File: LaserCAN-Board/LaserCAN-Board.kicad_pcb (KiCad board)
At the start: 4 copper layers, 25 x 25 mm, 58 parts, among them J2 TC2050-IDC-NL, Q1 Si2309CDS-T1-GE3, U1 TPS7A2033PDBVR, U2 VL53L1CXV0FY1, U3 M24C64-RMN6TP, U4 STM32F103C8Tx, U6 SN65HVD230, U9 TPS54202DDC, Y1 8MHz 20pF

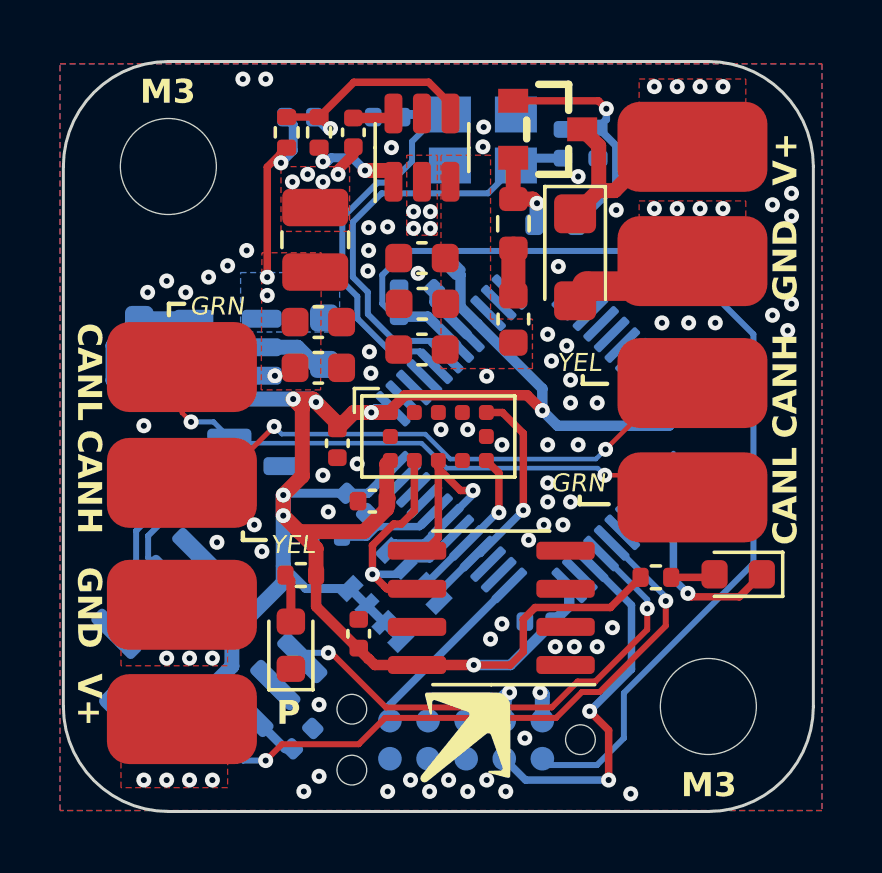
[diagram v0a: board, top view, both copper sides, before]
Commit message: Rev 4 updates - NPTH, improved routing, BOM optimisation
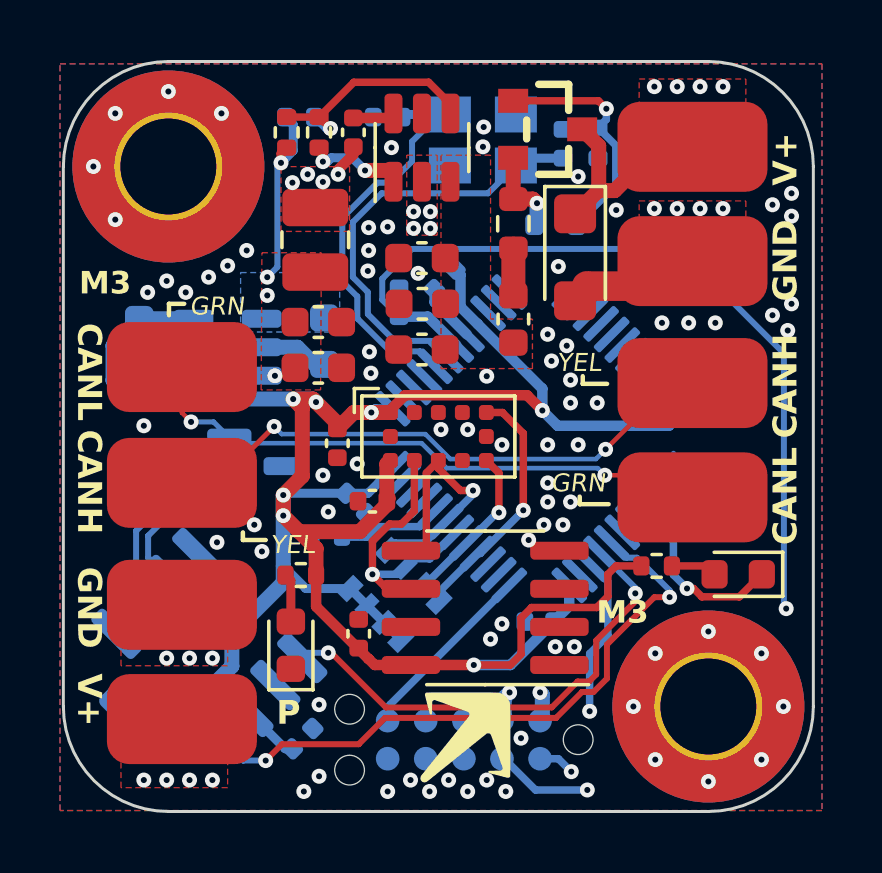
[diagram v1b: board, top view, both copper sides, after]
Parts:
- C20, C21: value 33pF -> 20pF
- H1, H2: footprint MountingHole:MountingHole_3.2mm_M3 -> MountingHole:MountingHole_3.2mm_M3_Pad_TopBottom
- Y1: value 8MHz 20pF -> 8MHz 12pF
- moved R6 0.38 mm to (139.8, 116.8)
- moved U3 0.20 mm to (134.1, 118.2)
- moved J2 0.08 mm to (135.9, 123.2)
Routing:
- net /NRST: track 36.1 -> 40.2 mm, vias 0 -> 2
- net /SWDIO: track 12.4 -> 11.8 mm
- net +3V3: track 88.8 -> 89.4 mm
- net /3V87: track 8.19 -> 7.60 mm
- net unconnected-(H2-Pad1): vias 0 -> 8
- net unconnected-(H1-Pad1): vias 0 -> 5
- net GND: vias 72 -> 67

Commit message: Start working on Rev5
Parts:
- R9: value 4.7 100mW -> 4.7
- moved RN1 0.52 mm to (130.6, 118.0)
- moved R10 0.18 mm to (128.7, 115.7)
- moved D4 0.08 mm to (126.5, 113.4)
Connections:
- net /SWDIO renamed /SWDIO/JTMS
- J2 pad 1: /NRST -> +12V
- J2 pad 10: +12V -> /NRST
- J2 pad 4: GND -> /SWCLK/JTCK
- J2 pad 6: /SWCLK -> /JTDO
- J2 pad 8: unconnected-(J2-Pad8) -> /JTDI
- J2 pad 9: +12V -> unconnected-(J2-Pad9)
- U4 pad 3: unconnected-(U4-PC14-Pad3) -> GND
- U4 pad 37: /SWCLK -> /SWCLK/JTCK
- U4 pad 38: unconnected-(U4-PA15-Pad38) -> /JTDI
- U4 pad 39: unconnected-(U4-PB3-Pad39) -> /JTDO
- U4 pad 40: /TOF_SHUT -> unconnected-(U4-PB4-Pad40)
- U4 pad 45: unconnected-(U4-PB8-Pad45) -> /TOF_SHUT
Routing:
- net /JTDI: track 0.00 -> 12.8 mm, vias 0 -> 1
- net /SWCLK/JTCK: track 0.00 -> 11.7 mm, vias 0 -> 3
- net /JTDO: track 0.00 -> 10.7 mm, vias 0 -> 1
- net /SWCLK: track 6.16 -> 0.00 mm
- net /TOF_SHUT: track 8.33 -> 12.7 mm, vias 1 -> 2
- net /NRST: track 40.2 -> 37.6 mm
- net +12V: track 65.9 -> 64.9 mm, vias 10 -> 9
- net /SWDIO/JTMS: track 11.8 -> 10.8 mm, vias 2 -> 1
- net /I2C_SCL: track 9.95 -> 10.8 mm
- net /I2C_SDA: track 8.64 -> 9.54 mm
- net /CAN_TX: track 16.1 -> 15.4 mm
- net +3V3: track 89.4 -> 88.8 mm
- net /TOF_INT: track 5.46 -> 6.03 mm
- net GND: vias 67 -> 62
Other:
- board text added: "LaserCAN Rev. 5"
- board text removed: "LaserCAN Rev. 4"

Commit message: Rev 5 Updates
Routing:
- net /JTDI: track 12.8 -> 5.53 mm, vias 1 -> 0
- net /SWCLK/JTCK: track 11.7 -> 7.47 mm, vias 3 -> 2
- net /JTDO: track 10.7 -> 6.60 mm, vias 1 -> 0
- net /SWDIO/JTMS: track 10.8 -> 9.81 mm, vias 1 -> 0
- net GND: vias 62 -> 64
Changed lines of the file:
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@@
   (via (at 123.444 107.315) (size 0.5) (drill 0.2) (layers "F.Cu" "B.Cu") (free) (net 1))
   (via (at 136.144 112.776) (size 0.5) (drill 0.2) (layers "F.Cu" "B.Cu") (free) (net 1))
+  (via (at 128.397 124.079) (size 0.5) (drill 0.2) (layers "F.Cu" "B.Cu") (free) (net 1))
   (via (at 143.637 108.458) (size 0.5) (drill 0.2) (layers "F.Cu" "B.Cu") (free) (net 1))
   (via (at 136.271 109.982) (size 0.5) (drill 0.2) (layers "F.Cu" "B.Cu") (free) (net 1))
@@
   (via (at 128.651 113.792) (size 0.5) (drill 0.2) (layers "F.Cu" "B.Cu") (free) (net 1))
   (via (at 133.096 123.952) (size 0.5) (drill 0.2) (layers "F.Cu" "B.Cu") (free) (net 1))
+  (via (at 138.176 124.079) (size 0.5) (drill 0.2) (layers "F.Cu" "B.Cu") (free) (net 1))
   (via (at 134.112 110.49) (size 0.5) (drill 0.2) (layers "F.Cu" "B.Cu") (free) (net 1))
   (via (at 136.398 119.507) (size 0.5) (drill 0.2) (layers "F.Cu" "B.Cu") (free) (net 1))
@@
   (via (at 140.462 100.838) (size 0.5) (drill 0.2) (layers "F.Cu" "B.Cu") (free) (net 3))
   (via (at 136.017 123.952) (size 0.5) (drill 0.2) (layers "F.Cu" "B.Cu") (net 3))
-  (segment (start 127.9457 122.6253) (end 127.504813 123.066187) (width 0.5) (layer "In2.Cu") (net 3))
+  (segment (start 128.293903 122.6253) (end 126.967203 123.952) (width 0.5) (layer "In2.Cu") (net 3))
+  (segment (start 135.27 123.205) (end 131.4718 123.205) (width 0.5) (layer "In2.Cu") (net 3))
   (segment (start 120.65 122.174) (end 120.65 107.823) (width 0.5) (layer "In2.Cu") (net 3))
-  (segment (start 127.124052 123.795151) (end 126.267849 123.795151) (width 0.5) (layer "In2.Cu") (net 3))
-  (segment (start 126.111 123.952) (end 124.968 123.952) (width 0.5) (layer "In2.Cu") (net 3))
-  (segment (start 127.504813 123.066187) (end 127.504813 123.41439) (width 0.5) (layer "In2.Cu") (net 3))
   (segment (start 120.65 107.823) (end 122.57 105.903) (width 0.5) (layer "In2.Cu") (net 3))
+  (segment (start 131.4718 123.205) (end 130.8921 122.6253) (width 0.5) (layer "In2.Cu") (net 3))
   (segment (start 125.8928 104.404162) (end 125.8928 102.580199) (width 0.5) (layer "In2.Cu") (net 3))
-  (segment (start 130.8921 122.6253) (end 127.9457 122.6253) (width 0.5) (layer "In2.Cu") (net 3))
-  (segment (start 135.27 123.205) (end 131.4718 123.205) (width 0.5) (layer "In2.Cu") (net 3))
   (segment (start 124.393962 105.903) (end 125.8928 104.404162) (width 0.5) (layer "In2.Cu") (net 3))
   (segment (start 124.968 123.952) (end 122.428 123.952) (width 0.5) (layer "In2.Cu") (net 3))
   (segment (start 122.428 123.952) (end 120.65 122.174) (width 0.5) (layer "In2.Cu") (net 3))
-  (segment (start 131.4718 123.205) (end 130.8921 122.6253) (width 0.5) (layer "In2.Cu") (net 3))
+  (segment (start 126.967203 123.952) (end 124.968 123.952) (width 0.5) (layer "In2.Cu") (net 3))
   (segment (start 127.635 100.838) (end 141.986 100.838) (width 0.5) (layer "In2.Cu") (net 3))
   (segment (start 136.017 123.952) (end 135.27 123.205) (width 0.5) (layer "In2.Cu") (net 3))
-  (segment (start 126.267849 123.795151) (end 126.111 123.952) (width 0.5) (layer "In2.Cu") (net 3))
-  (segment (start 127.504813 123.41439) (end 127.124052 123.795151) (width 0.5) (layer "In2.Cu") (net 3))
+  (segment (start 130.8921 122.6253) (end 128.293903 122.6253) (width 0.5) (layer "In2.Cu") (net 3))
   (segment (start 122.57 105.903) (end 124.393962 105.903) (width 0.5) (layer "In2.Cu") (net 3))
   (segment (start 125.8928 102.580199) (end 127.635 100.838) (width 0.5) (layer "In2.Cu") (net 3))
@@
   (segment (start 130.46037 115.50374) (end 130.109686 115.854424) (width 0.25) (layer "B.Cu") (net 13))
   (segment (start 131.873 115.50374) (end 130.46037 115.50374) (width 0.25) (layer "B.Cu") (net 13))
-  (via (at 135.128 123.9843) (size 0.5) (drill 0.2) (layers "F.Cu" "B.Cu") (net 15))
   (segment (start 138.43 118.783449) (end 138.43 117.613074) (width 0.1524) (layer "B.Cu") (net 15))
   (segment (start 137.198449 120.015) (end 138.43 118.783449) (width 0.1524) (layer "B.Cu") (net 15))
   (segment (start 134.62 123.2408) (end 134.0003 122.6211) (width 0.1524) (layer "B.Cu") (net 15))
   (segment (start 135.699411 120.015) (end 137.198449 120.015) (width 0.1524) (layer "B.Cu") (net 15))
-  (segment (start 134.62 123.2408) (end 134.62 123.4763) (width 0.1524) (layer "B.Cu") (net 15))
   (segment (start 138.43 117.613074) (end 137.570495 116.753569) (width 0.1524) (layer "B.Cu") (net 15))
-  (segment (start 134.62 123.4763) (end 135.128 123.9843) (width 0.1524) (layer "B.Cu") (net 15))
   (segment (start 134.0003 122.6211) (end 134.0003 121.714111) (width 0.1524) (layer "B.Cu") (net 15))
   (segment (start 134.0003 121.714111) (end 135.699411 120.015) (width 0.1524) (layer "B.Cu") (net 15))
@@
   (segment (start 132.851 119.488129) (end 133.721129 118.618) (width 0.2) (layer "F.Cu") (net 36))
   (via (at 132.851 119.488129) (size 0.5) (drill 0.2) (layers "F.Cu" "B.Cu") (net 36))
-  (via (at 128.471459 124.200025) (size 0.5) (drill 0.2) (layers "F.Cu" "B.Cu") (net 36))
   (via (at 133.731 118.618) (size 0.5) (drill 0.2) (layers "F.Cu" "B.Cu") (net 36))
   (segment (start 131.445 120.894129) (end 131.445 122.6058) (width 0.1524) (layer "B.Cu") (net 36))
-  (segment (start 128.713934 124.4425) (end 130.8783 124.4425) (width 0.1524) (layer "B.Cu") (net 36))
   (segment (start 131.445 122.6058) (end 132.08 123.2408) (width 0.1524) (layer "B.Cu") (net 36))
-  (segment (start 130.8783 124.4425) (end 132.08 123.2408) (width 0.1524) (layer "B.Cu") (net 36))
-  (segment (start 128.471459 124.200025) (end 128.713934 124.4425) (width 0.1524) (layer "B.Cu") (net 36))
   (segment (start 134.865812 117.483188) (end 133.731 118.618) (width 0.2) (layer "B.Cu") (net 36))
   (segment (start 134.865812 117.460676) (end 134.865812 117.483188) (width 0.2) (layer "B.Cu") (net 36))
   (segment (start 132.851 119.488129) (end 131.445 120.894129) (width 0.1524) (layer "B.Cu") (net 36))
-  (via (at 137.033 123.952) (size 0.5) (drill 0.2) (layers "F.Cu" "B.Cu") (net 37))
   (segment (start 134.512258 117.107122) (end 133.2548 118.36458) (width 0.1524) (layer "B.Cu") (net 37))
   (segment (start 133.204 121.8248) (end 133.35 121.9708) (width 0.1524) (layer "B.Cu") (net 37))
   (segment (start 133.204 119.907) (end 133.204 121.8248) (width 0.1524) (layer "B.Cu") (net 37))
-  (segment (start 132.6198 124.149249) (end 132.6198 123.754751) (width 0.1524) (layer "B.Cu") (net 37))
-  (segment (start 137.033 123.952) (end 136.525 124.46) (width 0.1524) (layer "B.Cu") (net 37))
   (segment (start 133.2548 118.36458) (end 133.2548 119.110851) (width 0.1524) (layer "B.Cu") (net 37))
-  (segment (start 132.930551 124.46) (end 132.6198 124.149249) (width 0.1524) (layer "B.Cu") (net 37))
-  (segment (start 132.715 122.999411) (end 133.35 122.364411) (width 0.1524) (layer "B.Cu") (net 37))
   (segment (start 133.2548 119.110851) (end 133.3267 119.182751) (width 0.1524) (layer "B.Cu") (net 37))
-  (segment (start 136.525 124.46) (end 132.930551 124.46) (width 0.1524) (layer "B.Cu") (net 37))
-  (segment (start 132.715 123.659551) (end 132.715 122.999411) (width 0.1524) (layer "B.Cu") (net 37))
-  (segment (start 133.35 122.364411) (end 133.35 121.9708) (width 0.1524) (layer "B.Cu") (net 37))
-  (segment (start 132.6198 123.754751) (end 132.715 123.659551) (width 0.1524) (layer "B.Cu") (net 37))
   (segment (start 133.3267 119.7843) (end 133.204 119.907) (width 0.1524) (layer "B.Cu") (net 37))
   (segment (start 133.3267 119.182751) (end 133.3267 119.7843) (width 0.1524) (layer "B.Cu") (net 37))
   (segment (start 134.6962 121.9479) (end 134.6962 121.9708) (width 0.5) (layer "B.Cu") (net 42))
-  (via (at 127.635 124.206) (size 0.5) (drill 0.2) (layers "F.Cu" "B.Cu") (net 43))
-  (segment (start 129.199641 122.7991) (end 129.9817 122.7991) (width 0.1524) (layer "B.Cu") (net 43))
-  (segment (start 129.9817 122.7991) (end 130.81 121.9708) (width 0.1524) (layer "B.Cu") (net 43))
   (segment (start 134.158705 116.753569) (end 134.158705 116.928647) (width 0.1524) (layer "B.Cu") (net 43))
   (segment (start 132.3748 118.712552) (end 132.3748 119.3392) (width 0.1524) (layer "B.Cu") (net 43))
-  (segment (start 127.635 124.206) (end 127.792741 124.206) (width 0.1524) (layer "B.Cu") (net 43))
   (segment (start 134.158705 116.928647) (end 132.3748 118.712552) (width 0.1524) (layer "B.Cu") (net 43))
   (segment (start 130.81 120.904) (end 130.81 121.9708) (width 0.1524) (layer "B.Cu") (net 43))
-  (segment (start 127.792741 124.206) (end 129.199641 122.7991) (width 0.1524) (layer "B.Cu") (net 43))
   (segment (start 132.3748 119.3392) (end 130.81 120.904) (width 0.1524) (layer "B.Cu") (net 43))
   (segment (start 134.994 103.2104) (end 134.994 104.578) (width 0.5) (layer "F.Cu") (net 47))

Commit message: Slight changes
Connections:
- J2 pad 1: +12V -> +3V3
- J2 pad 5: unconnected-(J2-Pad5) -> +12V
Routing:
- net +3V3: track 88.8 -> 94.6 mm, vias 7 -> 8
- net +12V: track 64.7 -> 59.8 mm
- net /SWDIO/JTMS: track 9.81 -> 8.96 mm
- net GND: vias 64 -> 65

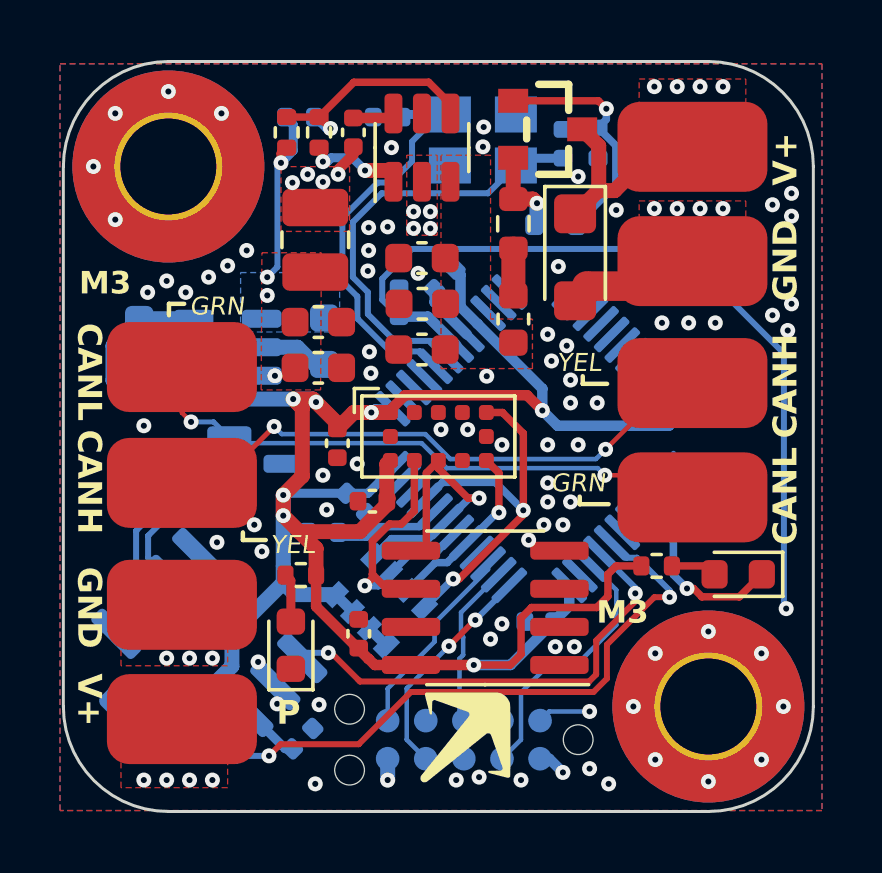
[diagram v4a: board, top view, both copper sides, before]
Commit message: Update to support new grplbndl flash method
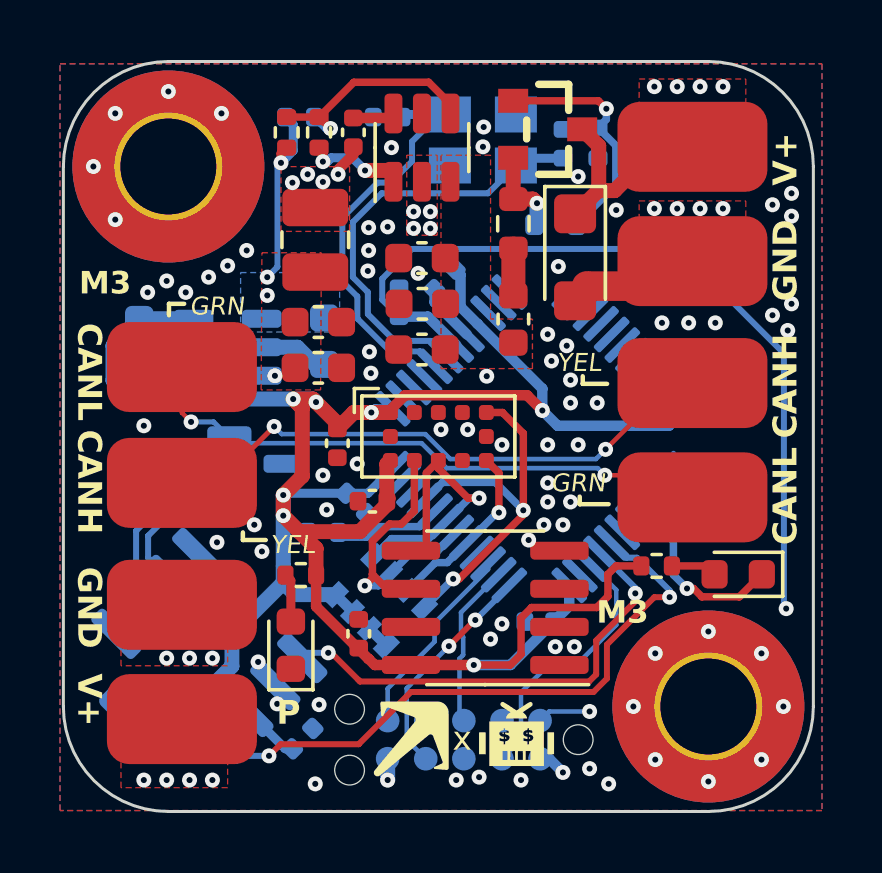
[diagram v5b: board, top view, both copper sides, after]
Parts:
- removed the G*** at (133.4, 122.5)
- added G***: LOGO, LOGO, F.Cu at (135.1, 122.4)
- added G***: LOGO, LOGO, F.Cu at (131.6, 122.6)
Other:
- board text added: "x"

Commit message: Bootloader v2 updates
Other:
- board text added: "LaserCAN Rev. 5U"
- board text added: "STACKUP: Top - .gtl (1oz copper) In1 - .g1 (0.5oz copper) In2 - .g2 (0.5oz copper) Bottom - .gbl (1oz copper) Thickness: 1.6mm FR4 Mask: Purple Silkscreen: White Finish: ENIG Min Via: 0.5mm/0.2mm Min Trace: 0.1524mm width Min Clearance: 0.09mm"
- board text removed: "LaserCAN Rev. 5"
